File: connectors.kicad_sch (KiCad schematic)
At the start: 4 parts

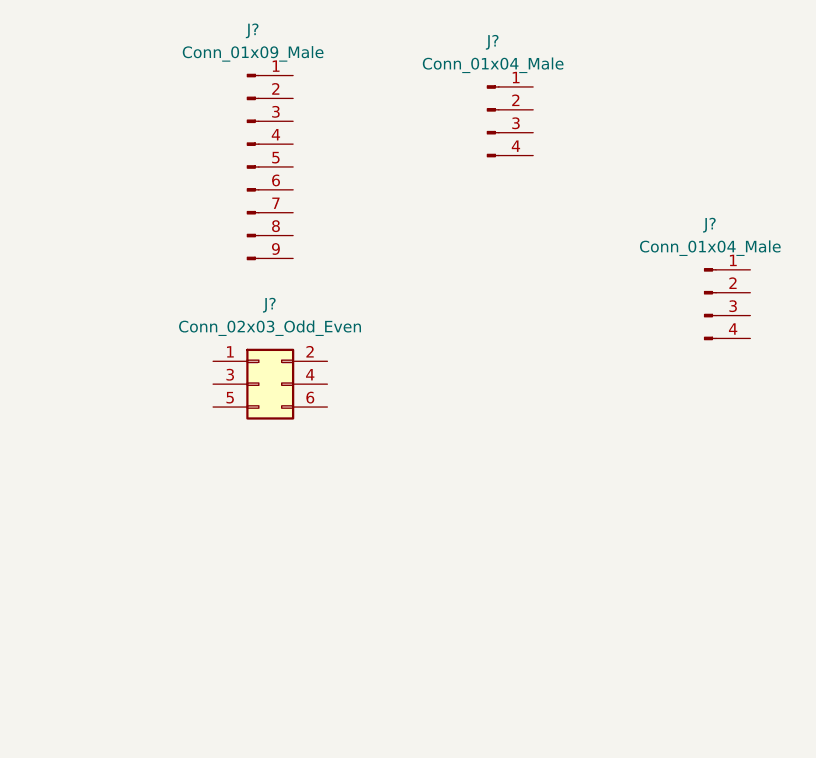
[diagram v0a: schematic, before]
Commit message: annotate symbol
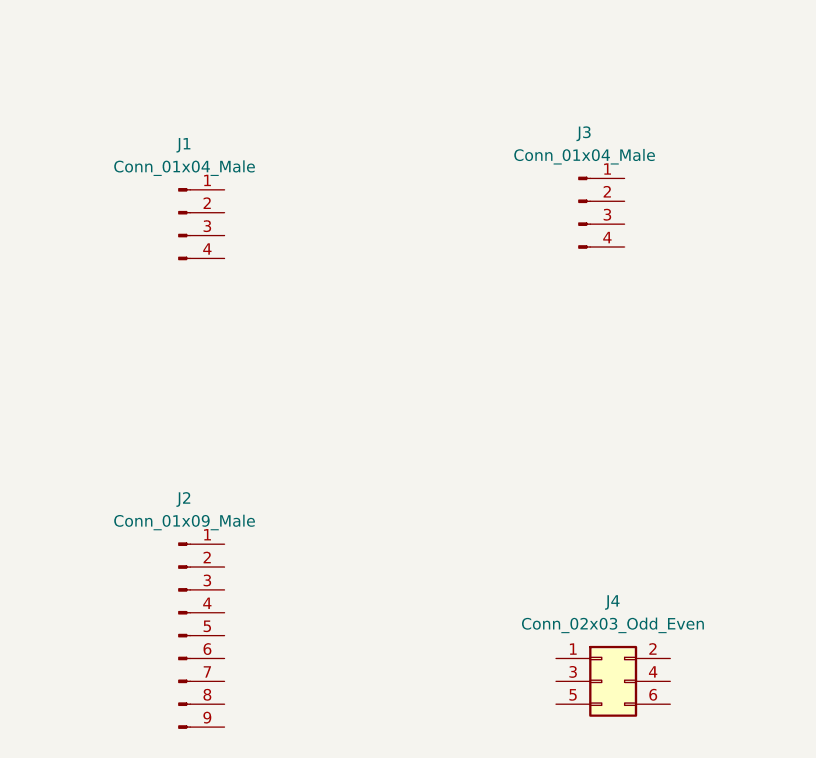
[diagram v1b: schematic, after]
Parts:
- gave numbers to parts that had none: 4
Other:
- moved on the sheet: J1, J2, J3, J4
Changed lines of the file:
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@@
     (comment 1 "Designed by Bernard")
   )
-  (symbol (lib_id "Connector:Conn_01x09_Male") (at 124.46 73.66 0) (unit 1)
+  (symbol (lib_id "Connector:Conn_01x09_Male") (at 116.84 125.73 0) (unit 1)
     (in_bom yes) (on_board yes) (fields_autoplaced)
-    (property "Reference" "J?" (id 0) (at 125.095 58.42 0))
-    (property "Value" "Conn_01x09_Male" (id 1) (at 125.095 60.96 0))
-    (property "Footprint" "" (id 2) (at 124.46 73.66 0)
+    (property "Reference" "J2" (id 0) (at 117.475 110.49 0))
+    (property "Value" "Conn_01x09_Male" (id 1) (at 117.475 113.03 0))
+    (property "Footprint" "" (id 2) (at 116.84 125.73 0)
       (effects (font (size 1.27 1.27)) hide)
     )
-    (property "Datasheet" "~" (id 3) (at 124.46 73.66 0)
+    (property "Datasheet" "~" (id 3) (at 116.84 125.73 0)
       (effects (font (size 1.27 1.27)) hide)
     )
@@
     (pin "9")
   )
-  (symbol (lib_id "Connector:Conn_01x04_Male") (at 151.13 67.31 0) (unit 1)
+  (symbol (lib_id "Connector:Conn_01x04_Male") (at 161.29 77.47 0) (unit 1)
     (in_bom yes) (on_board yes) (fields_autoplaced)
-    (property "Reference" "J?" (id 0) (at 151.765 59.69 0))
-    (property "Value" "Conn_01x04_Male" (id 1) (at 151.765 62.23 0))
-    (property "Footprint" "" (id 2) (at 151.13 67.31 0)
+    (property "Reference" "J3" (id 0) (at 161.925 69.85 0))
+    (property "Value" "Conn_01x04_Male" (id 1) (at 161.925 72.39 0))
+    (property "Footprint" "" (id 2) (at 161.29 77.47 0)
       (effects (font (size 1.27 1.27)) hide)
     )
-    (property "Datasheet" "~" (id 3) (at 151.13 67.31 0)
+    (property "Datasheet" "~" (id 3) (at 161.29 77.47 0)
       (effects (font (size 1.27 1.27)) hide)
     )
@@
     (pin "4")
   )
-  (symbol (lib_id "Connector_Generic:Conn_02x03_Odd_Even") (at 125.73 97.79 0) (unit 1)
+  (symbol (lib_id "Connector_Generic:Conn_02x03_Odd_Even") (at 163.83 130.81 0) (unit 1)
     (in_bom yes) (on_board yes) (fields_autoplaced)
-    (property "Reference" "J?" (id 0) (at 127 88.9 0))
-    (property "Value" "Conn_02x03_Odd_Even" (id 1) (at 127 91.44 0))
-    (property "Footprint" "" (id 2) (at 125.73 97.79 0)
+    (property "Reference" "J4" (id 0) (at 165.1 121.92 0))
+    (property "Value" "Conn_02x03_Odd_Even" (id 1) (at 165.1 124.46 0))
+    (property "Footprint" "" (id 2) (at 163.83 130.81 0)
       (effects (font (size 1.27 1.27)) hide)
     )
-    (property "Datasheet" "~" (id 3) (at 125.73 97.79 0)
+    (property "Datasheet" "~" (id 3) (at 163.83 130.81 0)
       (effects (font (size 1.27 1.27)) hide)
     )
@@
     (pin "6")
   )
-  (symbol (lib_id "Connector:Conn_01x04_Male") (at 175.26 87.63 0) (unit 1)
+  (symbol (lib_id "Connector:Conn_01x04_Male") (at 116.84 78.74 0) (unit 1)
     (in_bom yes) (on_board yes) (fields_autoplaced)
-    (property "Reference" "J?" (id 0) (at 175.895 80.01 0))
-    (property "Value" "Conn_01x04_Male" (id 1) (at 175.895 82.55 0))
-    (property "Footprint" "" (id 2) (at 175.26 87.63 0)
+    (property "Reference" "J1" (id 0) (at 117.475 71.12 0))
+    (property "Value" "Conn_01x04_Male" (id 1) (at 117.475 73.66 0))
+    (property "Footprint" "" (id 2) (at 116.84 78.74 0)
       (effects (font (size 1.27 1.27)) hide)
     )
-    (property "Datasheet" "~" (id 3) (at 175.26 87.63 0)
+    (property "Datasheet" "~" (id 3) (at 116.84 78.74 0)
       (effects (font (size 1.27 1.27)) hide)
     )

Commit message: added heirechy sheets and linked the component in eeschema
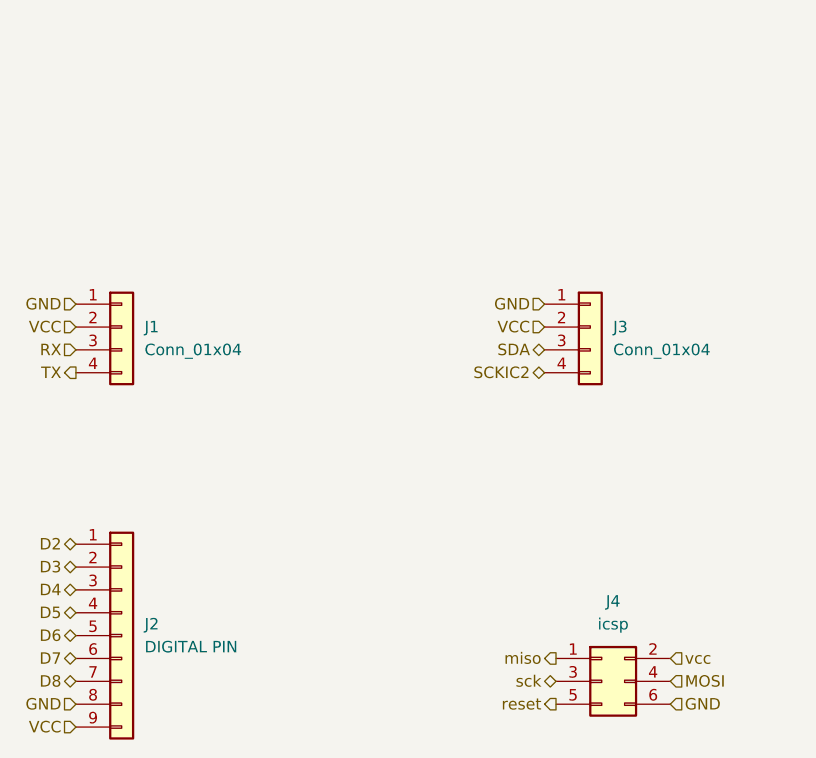
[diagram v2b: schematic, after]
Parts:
- removed J1, J3: Conn_01x04_Male, symbol Connector:Conn_01x04_Male
- removed J2: Conn_01x09_Male, symbol Connector:Conn_01x09_Male
- added J1, J3: Conn_01x04, Connector_PinSocket_2.54mm:PinSocket_1x04_P2.54mm_Vertical, symbol Connector_Generic:Conn_01x04
- added J2: DIGITAL PIN, Connector_PinSocket_2.54mm:PinSocket_1x09_P2.54mm_Vertical, symbol Connector_Generic:Conn_01x09
- J4: value Conn_02x03_Odd_Even -> icsp; footprint (none) -> Connector_PinSocket_2.54mm:PinSocket_2x03_P2.54mm_Vertical
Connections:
- net miso: now reaches J4.1 (Pin_1)
- net vcc: now reaches J4.2 (Pin_2)
- net sck: now reaches J4.3 (Pin_3)
- net MOSI: now reaches J4.4 (Pin_4)
- net reset: now reaches J4.5 (Pin_5)
- net GND: now reaches J4.6 (Pin_6)
- net GND: now also J1.1 (Pin_1), J2.8 (Pin_8), J3.1 (Pin_1)
- new net D2: J2.1 (Pin_1)
- new net D3: J2.2 (Pin_2)
- new net D4: J2.3 (Pin_3)
- new net D5: J2.4 (Pin_4)
- new net D6: J2.5 (Pin_5)
- new net D7: J2.6 (Pin_6)
- new net D8: J2.7 (Pin_7)
- new net RX: J1.3 (Pin_3)
- new net SCKIC2: J3.4 (Pin_4)
- new net SDA: J3.3 (Pin_3)
- new net TX: J1.4 (Pin_4)
- new net VCC: J1.2 (Pin_2), J2.9 (Pin_9), J3.2 (Pin_2)
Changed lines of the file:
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@@
     (comment 1 "Designed by Bernard")
   )
-  (symbol (lib_id "Connector:Conn_01x09_Male") (at 116.84 125.73 0) (unit 1)
+  (hierarchical_label "GND" (shape input) (at 157.48 88.9 180)
+    (effects (font (size 1.27 1.27)) (justify right))
+  )
+  (hierarchical_label "reset" (shape output) (at 158.75 133.35 180)
+    (effects (font (size 1.27 1.27)) (justify right))
+  )
+  (hierarchical_label "D3" (shape bidirectional) (at 105.41 118.11 180)
+    (effects (font (size 1.27 1.27)) (justify right))
+  )
+  (hierarchical_label "MOSI" (shape input) (at 171.45 130.81 0)
+    (effects (font (size 1.27 1.27)) (justify left))
+  )
+  (hierarchical_label "SDA" (shape bidirectional) (at 157.48 93.98 180)
+    (effects (font (size 1.27 1.27)) (justify right))
+  )
+  (hierarchical_label "D2" (shape bidirectional) (at 105.41 115.57 180)
+    (effects (font (size 1.27 1.27)) (justify right))
+  )
+  (hierarchical_label "VCC" (shape input) (at 105.41 91.44 180)
+    (effects (font (size 1.27 1.27)) (justify right))
+  )
+  (hierarchical_label "VCC" (shape input) (at 157.48 91.44 180)
+    (effects (font (size 1.27 1.27)) (justify right))
+  )
+  (hierarchical_label "GND" (shape input) (at 105.41 133.35 180)
+    (effects (font (size 1.27 1.27)) (justify right))
+  )
+  (hierarchical_label "D4" (shape bidirectional) (at 105.41 120.65 180)
+    (effects (font (size 1.27 1.27)) (justify right))
+  )
+  (hierarchical_label "vcc" (shape input) (at 171.45 128.27 0)
+    (effects (font (size 1.27 1.27)) (justify left))
+  )
+  (hierarchical_label "D8" (shape bidirectional) (at 105.41 130.81 180)
+    (effects (font (size 1.27 1.27)) (justify right))
+  )
+  (hierarchical_label "RX" (shape input) (at 105.41 93.98 180)
+    (effects (font (size 1.27 1.27)) (justify right))
+  )
+  (hierarchical_label "miso" (shape output) (at 158.75 128.27 180)
+    (effects (font (size 1.27 1.27)) (justify right))
+  )
+  (hierarchical_label "GND" (shape input) (at 171.45 133.35 0)
+    (effects (font (size 1.27 1.27)) (justify left))
+  )
+  (hierarchical_label "D7" (shape bidirectional) (at 105.41 128.27 180)
+    (effects (font (size 1.27 1.27)) (justify right))
+  )
+  (hierarchical_label "D6" (shape bidirectional) (at 105.41 125.73 180)
+    (effects (font (size 1.27 1.27)) (justify right))
+  )
+  (hierarchical_label "TX" (shape output) (at 105.41 96.52 180)
+    (effects (font (size 1.27 1.27)) (justify right))
+  )
+  (hierarchical_label "SCKIC2" (shape bidirectional) (at 157.48 96.52 180)
+    (effects (font (size 1.27 1.27)) (justify right))
+  )
+  (hierarchical_label "D5" (shape bidirectional) (at 105.41 123.19 180)
+    (effects (font (size 1.27 1.27)) (justify right))
+  )
+  (hierarchical_label "VCC" (shape input) (at 105.41 135.89 180)
+    (effects (font (size 1.27 1.27)) (justify right))
+  )
+  (hierarchical_label "GND" (shape input) (at 105.41 88.9 180)
+    (effects (font (size 1.27 1.27)) (justify right))
+  )
+  (hierarchical_label "sck" (shape bidirectional) (at 158.75 130.81 180)
+    (effects (font (size 1.27 1.27)) (justify right))
+  )
+  (symbol (lib_id "Connector_Generic:Conn_01x09") (at 110.49 125.73 0) (unit 1)
     (in_bom yes) (on_board yes) (fields_autoplaced)
-    (property "Reference" "J2" (id 0) (at 117.475 110.49 0))
-    (property "Value" "Conn_01x09_Male" (id 1) (at 117.475 113.03 0))
-    (property "Footprint" "" (id 2) (at 116.84 125.73 0)
+    (property "Reference" "J2" (id 0) (at 113.03 124.4599 0)
+      (effects (font (size 1.27 1.27)) (justify left))
+    )
+    (property "Value" "DIGITAL PIN" (id 1) (at 113.03 126.9999 0)
+      (effects (font (size 1.27 1.27)) (justify left))
+    )
+    (property "Footprint" "Connector_PinSocket_2.54mm:PinSocket_1x09_P2.54mm_Vertical" (id 2) (at 110.49 125.73 0)
       (effects (font (size 1.27 1.27)) hide)
     )
-    (property "Datasheet" "~" (id 3) (at 116.84 125.73 0)
+    (property "Datasheet" "~" (id 3) (at 110.49 125.73 0)
       (effects (font (size 1.27 1.27)) hide)
     )
@@
     (pin "9")
   )
-  (symbol (lib_id "Connector:Conn_01x04_Male") (at 161.29 77.47 0) (unit 1)
-    (in_bom yes) (on_board yes) (fields_autoplaced)
-    (property "Reference" "J3" (id 0) (at 161.925 69.85 0))
-    (property "Value" "Conn_01x04_Male" (id 1) (at 161.925 72.39 0))
-    (property "Footprint" "" (id 2) (at 161.29 77.47 0)
-      (effects (font (size 1.27 1.27)) hide)
-    )
-    (property "Datasheet" "~" (id 3) (at 161.29 77.47 0)
-      (effects (font (size 1.27 1.27)) hide)
-    )
-    (pin "1")
-    (pin "2")
-    (pin "3")
-    (pin "4")
-  )
   (symbol (lib_id "Connector_Generic:Conn_02x03_Odd_Even") (at 163.83 130.81 0) (unit 1)
     (in_bom yes) (on_board yes) (fields_autoplaced)
     (property "Reference" "J4" (id 0) (at 165.1 121.92 0))
-    (property "Value" "Conn_02x03_Odd_Even" (id 1) (at 165.1 124.46 0))
-    (property "Footprint" "" (id 2) (at 163.83 130.81 0)
+    (property "Value" "icsp" (id 1) (at 165.1 124.46 0))
+    (property "Footprint" "Connector_PinSocket_2.54mm:PinSocket_2x03_P2.54mm_Vertical" (id 2) (at 163.83 130.81 0)
       (effects (font (size 1.27 1.27)) hide)
     )
@@
     (pin "6")
   )
-  (symbol (lib_id "Connector:Conn_01x04_Male") (at 116.84 78.74 0) (unit 1)
+  (symbol (lib_id "Connector_Generic:Conn_01x04") (at 162.56 91.44 0) (unit 1)
     (in_bom yes) (on_board yes) (fields_autoplaced)
-    (property "Reference" "J1" (id 0) (at 117.475 71.12 0))
-    (property "Value" "Conn_01x04_Male" (id 1) (at 117.475 73.66 0))
-    (property "Footprint" "" (id 2) (at 116.84 78.74 0)
+    (property "Reference" "J3" (id 0) (at 165.1 91.4399 0)
+      (effects (font (size 1.27 1.27)) (justify left))
+    )
+    (property "Value" "Conn_01x04" (id 1) (at 165.1 93.9799 0)
+      (effects (font (size 1.27 1.27)) (justify left))
+    )
+    (property "Footprint" "Connector_PinSocket_2.54mm:PinSocket_1x04_P2.54mm_Vertical" (id 2) (at 162.56 91.44 0)
       (effects (font (size 1.27 1.27)) hide)
     )
-    (property "Datasheet" "~" (id 3) (at 116.84 78.74 0)
+    (property "Datasheet" "~" (id 3) (at 162.56 91.44 0)
       (effects (font (size 1.27 1.27)) hide)
     )
+    (pin "1")
+    (pin "2")
+    (pin "3")
+    (pin "4")
+  )
+  (symbol (lib_id "Connector_Generic:Conn_01x04") (at 110.49 91.44 0) (unit 1)
+    (in_bom yes) (on_board yes) (fields_autoplaced)
+    (property "Reference" "J1" (id 0) (at 113.03 91.4399 0)
+      (effects (font (size 1.27 1.27)) (justify left))
+    )
+    (property "Value" "Conn_01x04" (id 1) (at 113.03 93.9799 0)
+      (effects (font (size 1.27 1.27)) (justify left))
+    )
+    (property "Footprint" "Connector_PinSocket_2.54mm:PinSocket_1x04_P2.54mm_Vertical" (id 2) (at 110.49 91.44 0)
+      (effects (font (size 1.27 1.27)) hide)
+    )
+    (property "Datasheet" "~" (id 3) (at 110.49 91.44 0)
+      (effects (font (size 1.27 1.27)) hide)
+    )
